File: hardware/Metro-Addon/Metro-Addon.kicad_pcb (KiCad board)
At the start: 2 copper layers, 50.8 x 33.2 mm, 16 parts, among them J1 Conn_02x03_Odd_Even, SW1 SW_RST, SW2 On, U1 PY32F002AA15M6TU

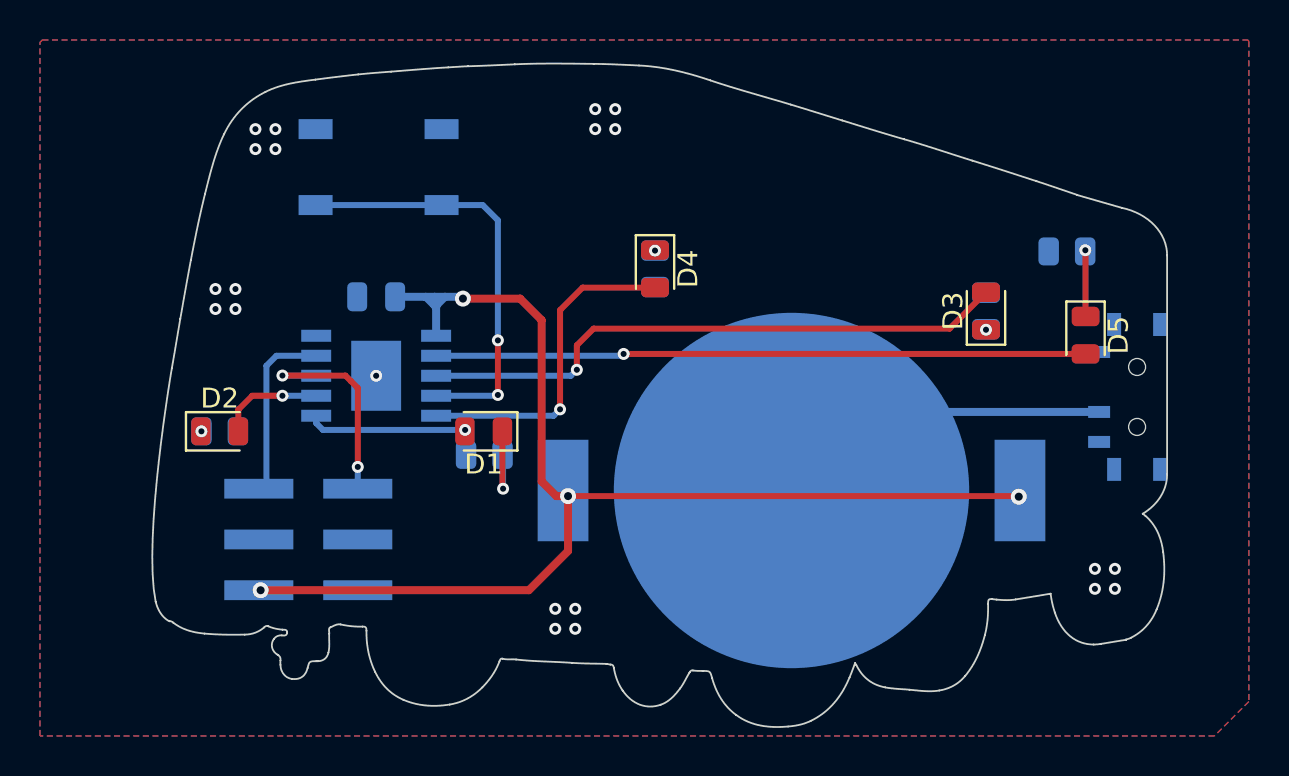
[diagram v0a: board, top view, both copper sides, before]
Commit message: feat(Hw):Labels-Added
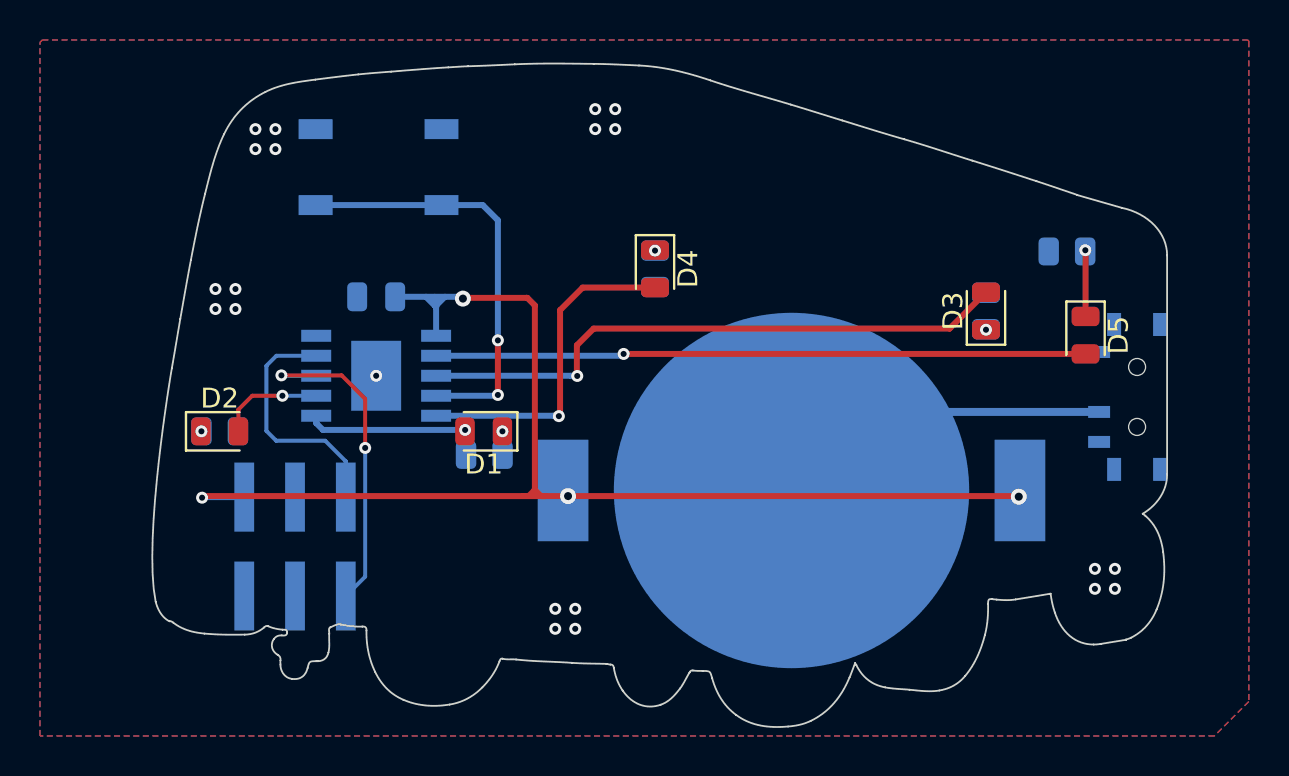
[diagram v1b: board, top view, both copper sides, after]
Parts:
- added kibuzzard-684752D8: G***, kibuzzard-684752D8, B.Cu at (155.0, 127.2)
- added kibuzzard-684752FB: G***, kibuzzard-684752FB, B.Cu at (155.0, 122.4)
- added kibuzzard-684756AF: G***, kibuzzard-684756AF, B.Cu at (143.8, 121.5)
- added kibuzzard-684756BD: G***, kibuzzard-684756BD, B.Cu at (143.9, 127.3)
- added kibuzzard-684756E4: G***, kibuzzard-684756E4, B.Cu at (188.6, 112.9)
- added kibuzzard-684756F0: G***, kibuzzard-684756F0, B.Cu at (188.4, 123.0)
- moved J1 5.40 mm to (151.5, 127.4), turned to 0 degrees
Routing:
- net /SWDIO: track 10.8 -> 16.7 mm
- net Net-(D1-K): track 4.58 -> 1.18 mm
- net /SWCLK: track 9.00 -> 12.3 mm
- net +3.3V: track 62.8 -> 64.6 mm

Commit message: feat(Hw):Led_Modified
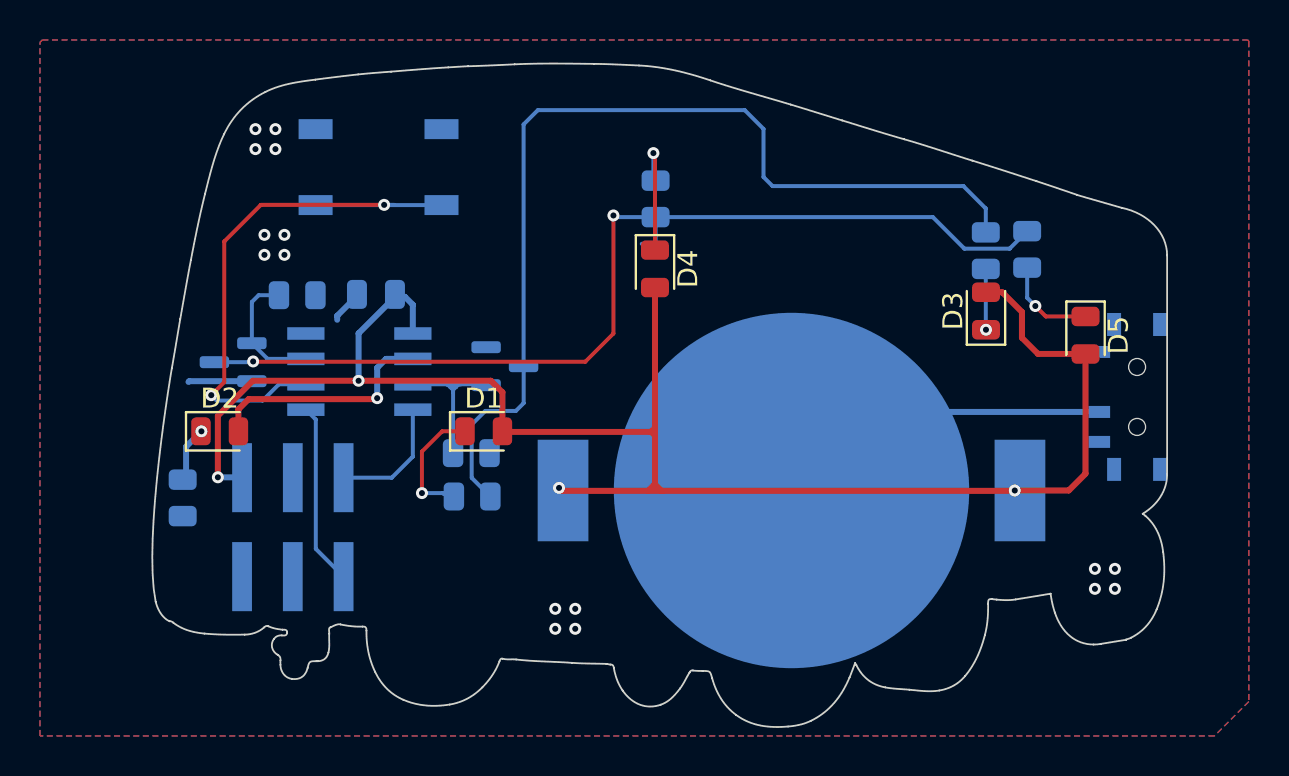
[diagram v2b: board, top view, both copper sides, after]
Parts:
- removed R2, R3, R5: 330R, Resistor_SMD:R_0805_2012Metric
- added Q1: 2N7002, Package_TO_SOT_SMD:SOT-23, B.Cu at (145.9, 115.7)
- added Q2: 2N7002, Package_TO_SOT_SMD:SOT-23, B.Cu at (159.5, 115.9)
- added R10: 180R, Resistor_SMD:R_0805_2012Metric, B.Cu at (157.8, 122.4)
- added R6: 100K, Resistor_SMD:R_0805_2012Metric, B.Cu at (149.1, 112.3)
- added R7: 180R, Resistor_SMD:R_0805_2012Metric, B.Cu at (167.0, 107.5)
- added R8: 100K, Resistor_SMD:R_0805_2012Metric, B.Cu at (157.8, 120.2)
- added R9: 180R, Resistor_SMD:R_0805_2012Metric, B.Cu at (183.5, 110.1)
- R1, R4: value 330R -> 180R
- U1: footprint Library:PY32F002AA15M -> Library:PY32F002AL15S6TU
- moved R4 18.6 mm to (185.6, 110.0)
- moved R1 15.2 mm to (143.4, 122.5), turned to 90 degrees
- moved kibuzzard-684756AF 1.68 mm to (143.3, 120.0)
- moved J1 0.98 mm to (151.4, 126.4)
- moved U1 0.87 mm to (152.2, 116.1)
- moved kibuzzard-684756BD 0.63 mm to (143.3, 127.1)
- moved C1 0.12 mm to (153.0, 112.3)
- turned D1 to 0 degrees
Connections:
- D1 pad 2: /PA6 -> +3.3V
- D2 pad 2: /PA7 -> /PA4
- D3 pad 2: /PA5 -> +3.3V
- D4 pad 2: /PA1 -> +3.3V
- D5 pad 2: /PF0 -> +3.3V
- R1 pad 2: Net-(D1-K) -> Net-(D2-K)
- R4 pad 1: GND -> Net-(D5-K)
- R4 pad 2: Net-(D4-K) -> Net-(Q1-D)
- U1 pad 2: /PF0 -> /PA4
- U1 pad 3: /PA5 -> /PA3
- U1 pad 4: /NRST -> /SWCLK
- U1 pad 5: /PA1 -> /SWDIO
- U1 pad 6: /PA6 -> /NRST
- U1 pad 7: /PA7 -> /PA1
- U1 pad 8: /SWDIO -> GND
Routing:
- net Net-(Q1-D): track 0.00 -> 50.7 mm, vias 0 -> 2
- net Net-(Q2-D): track 0.00 -> 49.0 mm
- net /PF0: track 32.5 -> 0.00 mm, vias 1 -> 0
- net /PA5: track 30.2 -> 0.00 mm, vias 1 -> 0
- net +3.3V: track 64.6 -> 88.5 mm
- net /PA4: track 0.00 -> 11.8 mm, vias 0 -> 1
- net /PA1: track 16.7 -> 6.59 mm, vias 1 -> 0
- net /PA3: track 0.00 -> 8.08 mm
- net /PA6: track 8.03 -> 0.00 mm, vias 1 -> 0
- net /SWDIO: track 16.7 -> 9.14 mm, vias 2 -> 0
- net /NRST: track 21.3 -> 28.7 mm
- net Net-(D4-K): track 0.00 -> 6.31 mm
- net /SWCLK: track 12.3 -> 6.25 mm
- net /PA7: track 5.27 -> 0.00 mm, vias 1 -> 0
- net Net-(D1-K): track 1.18 -> 6.32 mm
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
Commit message: feat(Hw):Mounting_Hole_Added
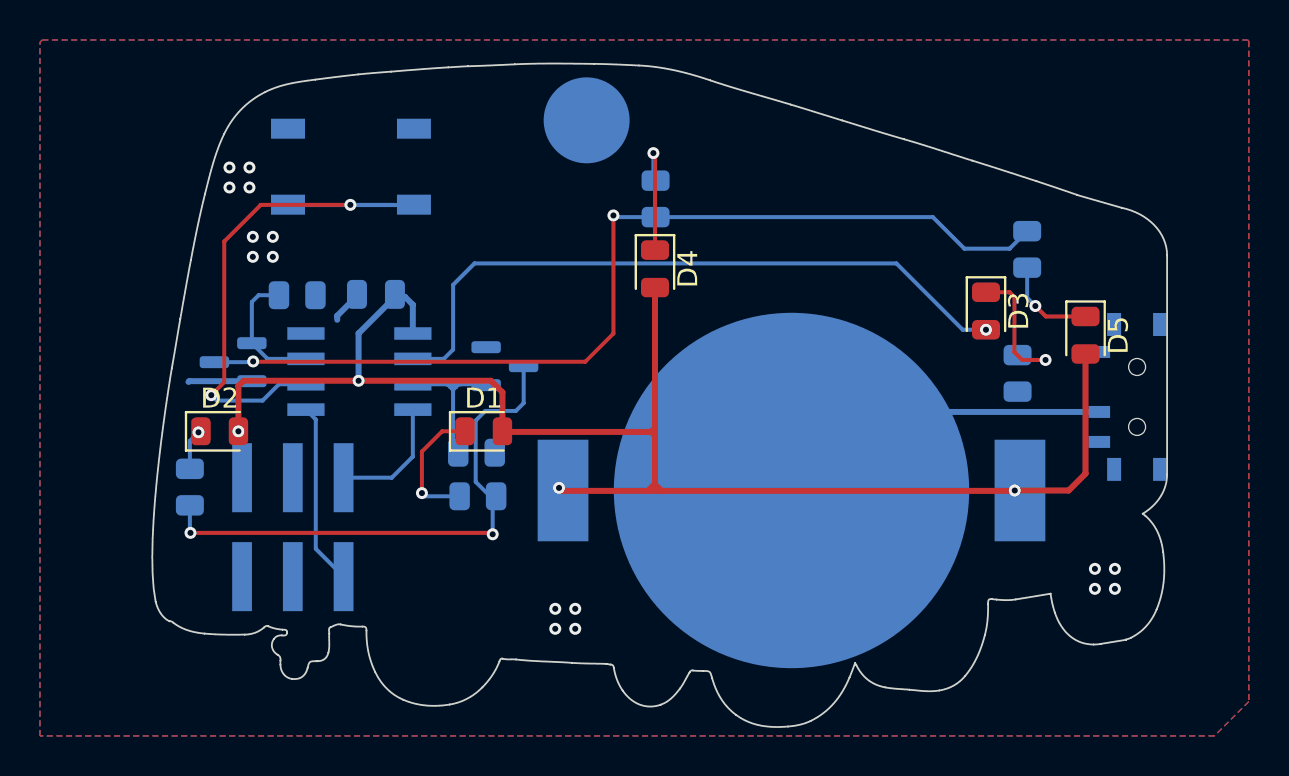
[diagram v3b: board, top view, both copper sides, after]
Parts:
- added REF**: MountingHole_4.3mm_M4, MountingHole:MountingHole_4.3mm_M4, F.Cu at (163.6, 103.4)
- moved R1 42.2 mm to (185.1, 116.2)
- moved R9 41.5 mm to (143.7, 121.9), turned to -90 degrees
- moved SW1 1.38 mm to (151.8, 105.9)
- moved R10 0.29 mm to (158.1, 122.4)
- moved R8 0.26 mm to (158.1, 120.2)
- turned D3 to -90 degrees
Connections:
- D2 pad 2: /PA4 -> +3.3V
- D3 pad 2: +3.3V -> /PA4
- R1 pad 2: Net-(D2-K) -> Net-(D3-K)
- R9 pad 1: Net-(D3-K) -> Net-(D2-K)
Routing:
- net /PA4: track 11.8 -> 33.9 mm
- net Net-(Q2-D): track 49.0 -> 27.5 mm, vias 0 -> 2
- net +3.3V: track 88.5 -> 80.2 mm
- net Net-(D3-K): track 3.05 -> 7.50 mm
- net Net-(Q1-D): track 50.7 -> 48.2 mm
- net Net-(D2-K): track 2.81 -> 2.15 mm
